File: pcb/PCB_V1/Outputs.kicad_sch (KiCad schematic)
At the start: 21 parts, among them J501 FAN1 / 3.5 mm, J511 FAN2 / 3.5 mm, J521 PUMP 24V / 6W, Q501 AO3400A, Q511 AO3400A, Q521 AO3422

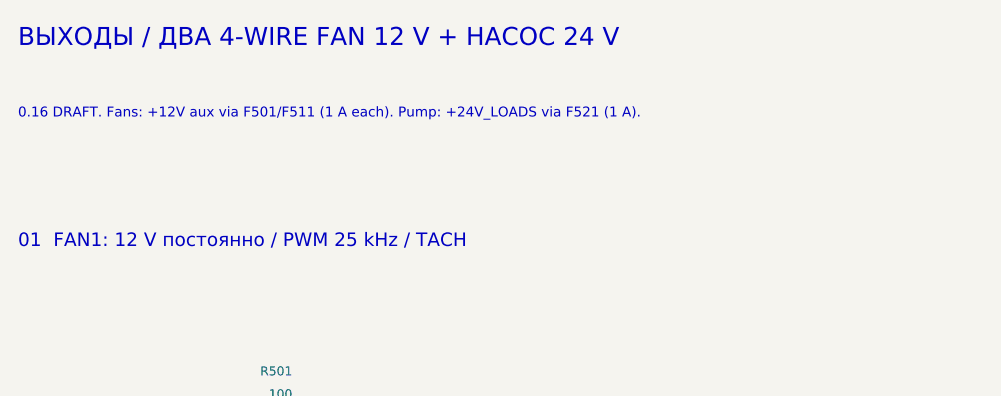
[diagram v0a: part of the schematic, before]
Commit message: pcb: integrate reviewed parts and validate initial 100mm placement
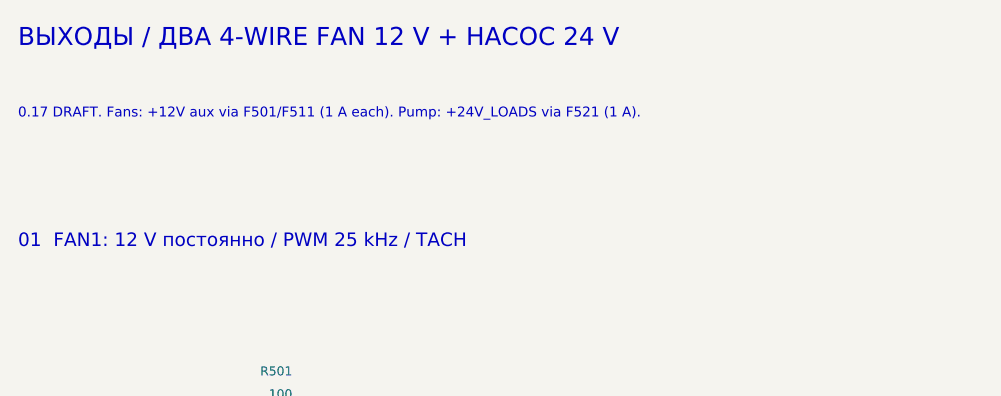
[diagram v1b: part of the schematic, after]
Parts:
- J501, J511: footprint TerminalBlock_Phoenix:TerminalBlock_Phoenix_PT-1,5-4-3.5-H_1x04_P3.50mm_Horizontal -> GrowBox:TerminalBlock_DORABO_DB125-3.5_1x04_P3.50mm_Horizontal
- J521: footprint TerminalBlock_Phoenix:TerminalBlock_Phoenix_PT-1,5-2-3.5-H_1x02_P3.50mm_Horizontal -> GrowBox:TerminalBlock_DORABO_DB125-3.5_1x02_P3.50mm_Horizontal
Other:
- note added: "0.17 DRAFT. Fans: +12V aux via F501/F511 (1 A each). Pump: +24V_LOADS via F521 (1 A)."
- note removed: "0.16 DRAFT. Fans: +12V aux via F501/F511 (1 A each). Pump: +24V_LOADS via F521 (1 A)."
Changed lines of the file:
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@@
 	(title_block
 		(title "04 - Fans (12 V aux) and pump (24 V)")
-		(date "2026-09-27")
-		(rev "0.16-DRAFT")
+		(date "2026-09-28")
+		(rev "0.17-DRAFT")
 		(company "GrowBox controller")
 		(comment 1 "Engineering draft; startup, thermal and fault qualification pending")
@@
 		)
 	)
-	(text "0.16 DRAFT. Fans: +12V aux via F501/F511 (1 A each). Pump: +24V_LOADS via F521 (1 A)."
+	(text "0.17 DRAFT. Fans: +12V aux via F501/F511 (1 A each). Pump: +24V_LOADS via F521 (1 A)."
 		(exclude_from_sim no)
 		(at 20.32 24.13 0)
@@
 			)
 		)
-		(property "Footprint" "TerminalBlock_Phoenix:TerminalBlock_Phoenix_PT-1,5-4-3.5-H_1x04_P3.50mm_Horizontal"
+		(property "Footprint" "GrowBox:TerminalBlock_DORABO_DB125-3.5_1x04_P3.50mm_Horizontal"
 			(at 182.88 60.96 0)
 			(hide yes)
@@
 			)
 		)
-		(property "Footprint" "TerminalBlock_Phoenix:TerminalBlock_Phoenix_PT-1,5-2-3.5-H_1x02_P3.50mm_Horizontal"
+		(property "Footprint" "GrowBox:TerminalBlock_DORABO_DB125-3.5_1x02_P3.50mm_Horizontal"
 			(at 185.42 191.77 0)
 			(hide yes)
@@
 			)
 		)
-		(property "Footprint" "TerminalBlock_Phoenix:TerminalBlock_Phoenix_PT-1,5-4-3.5-H_1x04_P3.50mm_Horizontal"
+		(property "Footprint" "GrowBox:TerminalBlock_DORABO_DB125-3.5_1x04_P3.50mm_Horizontal"
 			(at 381 60.96 0)
 			(hide yes)

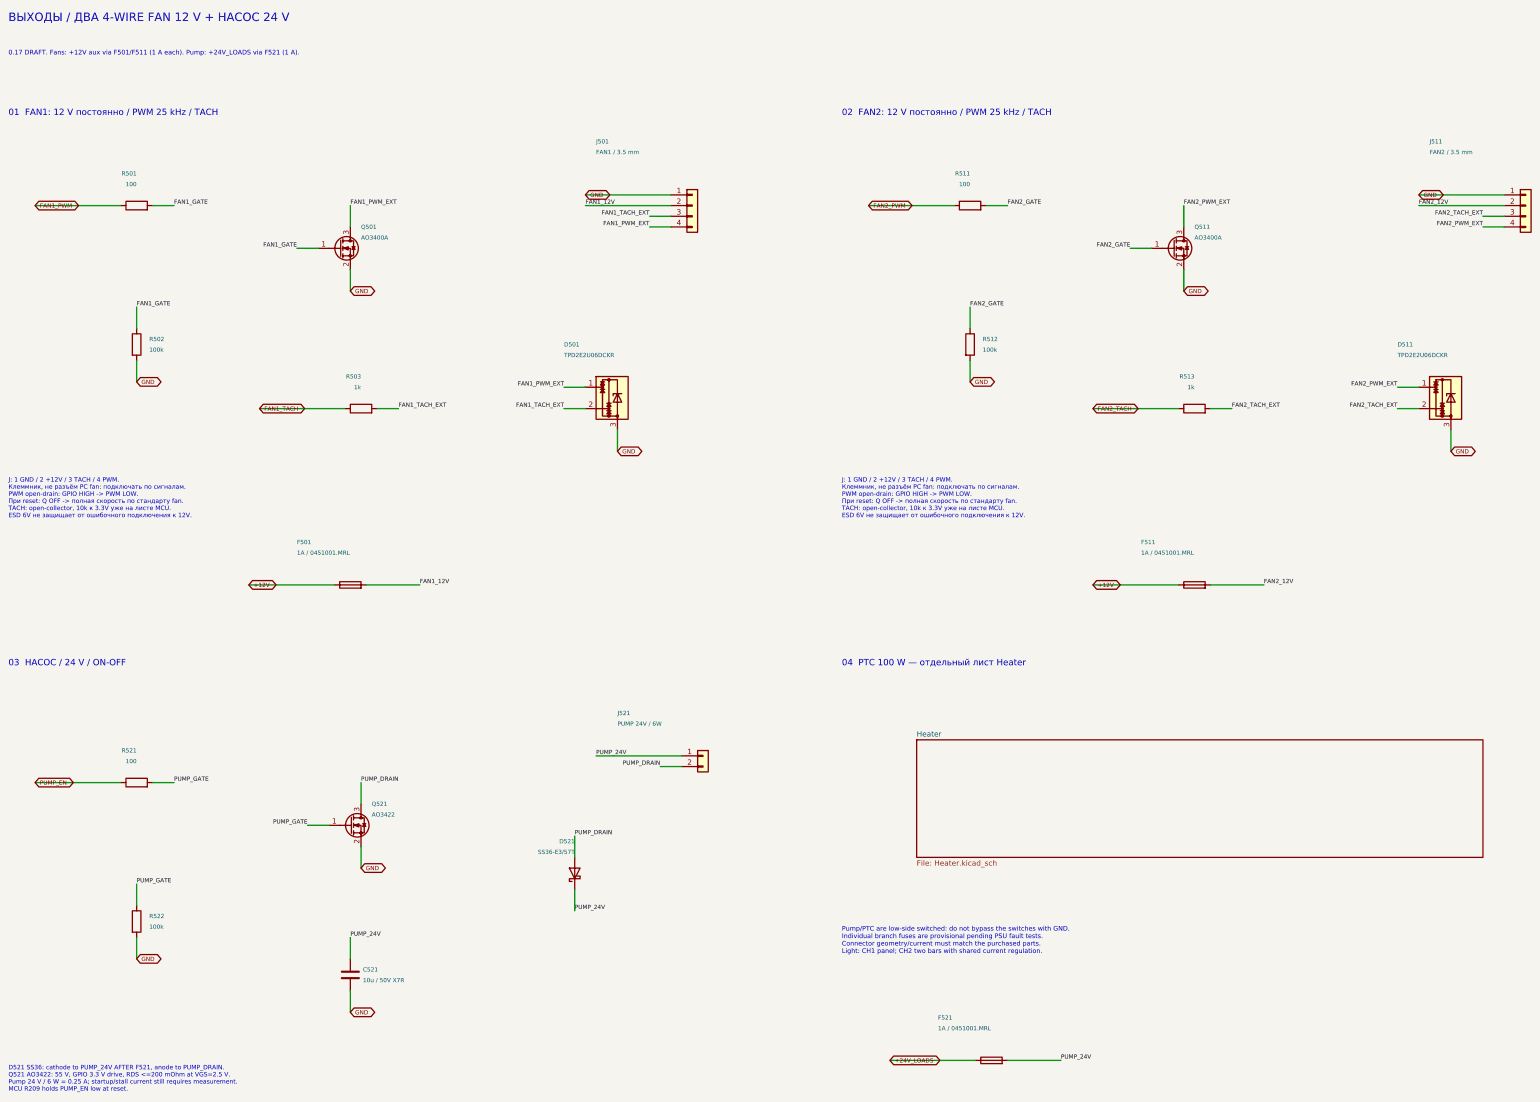
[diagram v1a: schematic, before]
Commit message: pcb: simplify passives and microSD circuitry for revision 0.18
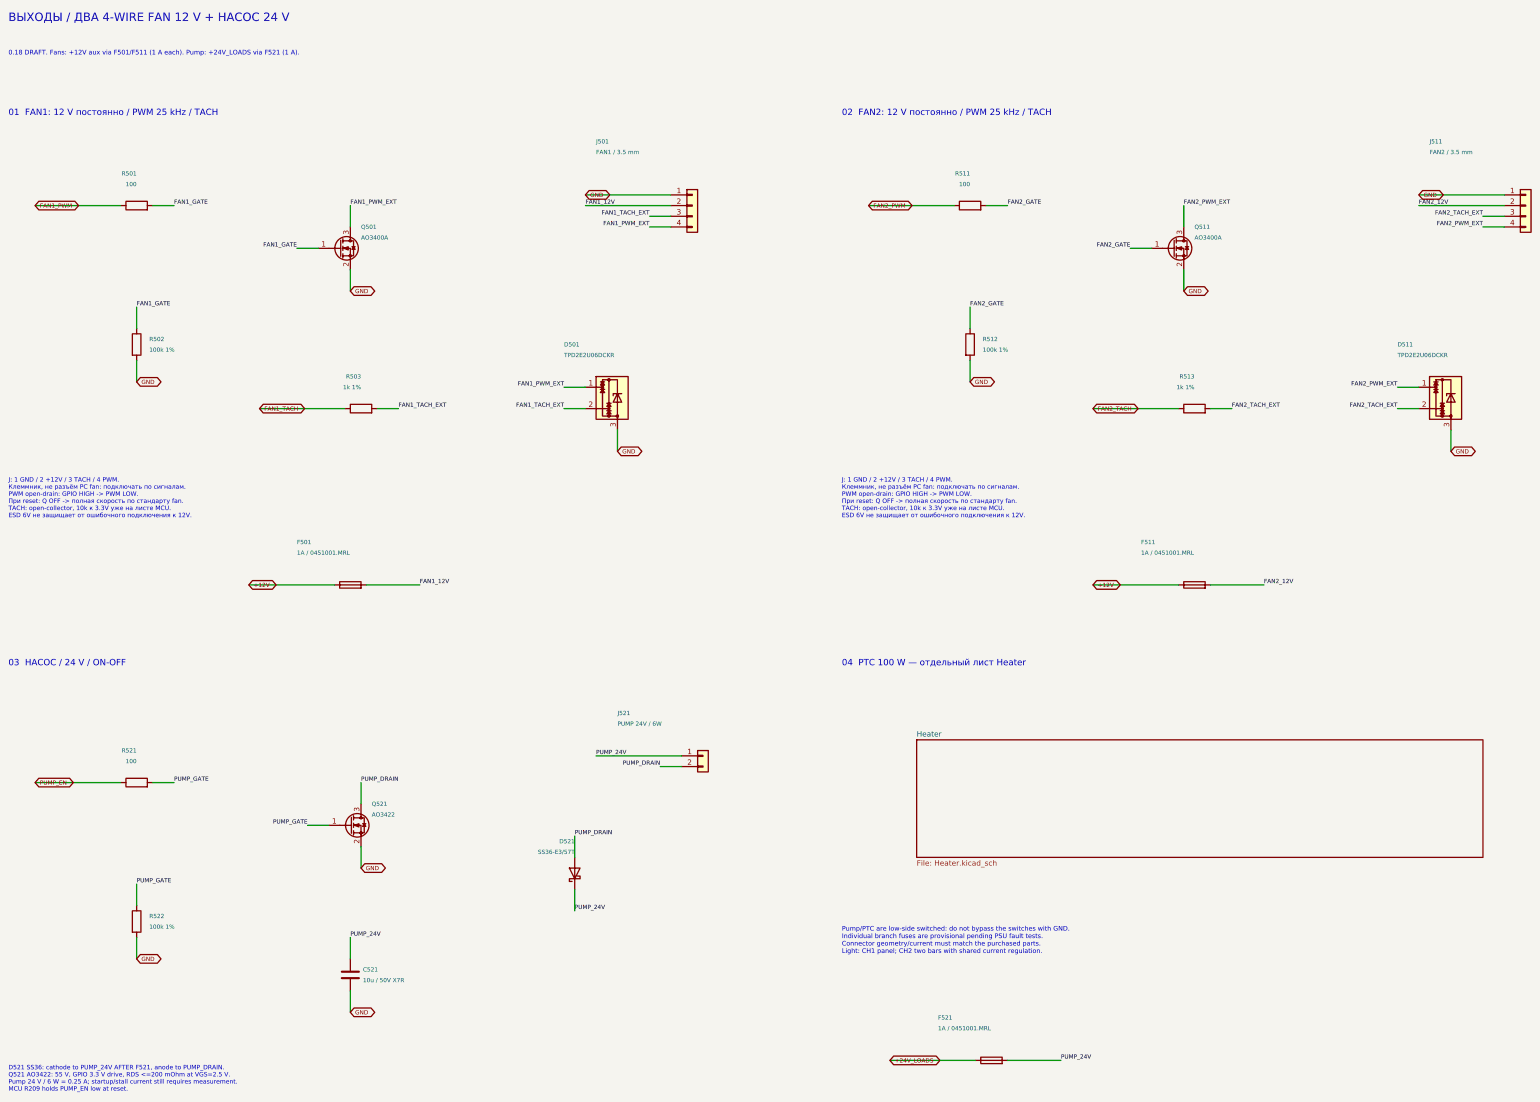
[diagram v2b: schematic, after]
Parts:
- R502, R512, R522: value 100k -> 100k 1%; LCSC (none) -> C25803; MPN (none) -> 0603WAF1003T5E; Manufacturer (none) -> UNI-ROYAL
- R503, R513: value 1k -> 1k 1%; LCSC (none) -> C21190; MPN (none) -> 0603WAF1001T5E; Manufacturer (none) -> UNI-ROYAL
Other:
- note added: "0.18 DRAFT. Fans: +12V aux via F501/F511 (1 A each). Pump: +24V_LOADS via F521 (1 A)."
- note removed: "0.17 DRAFT. Fans: +12V aux via F501/F511 (1 A each). Pump: +24V_LOADS via F521 (1 A)."
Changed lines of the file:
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@@
 	(title_block
 		(title "04 - Fans (12 V aux) and pump (24 V)")
-		(date "2026-09-28")
-		(rev "0.17-DRAFT")
+		(date "2026-09-29")
+		(rev "0.18-DRAFT")
 		(company "GrowBox controller")
-		(comment 1 "Engineering draft; startup, thermal and fault qualification pending")
+		(comment 1 "Simplified prototype; unrouted; hardware qualification pending")
 	)
 	(text "04  PTC 100 W — отдельный лист Heater"
@@
 		)
 	)
-	(text "0.17 DRAFT. Fans: +12V aux via F501/F511 (1 A each). Pump: +24V_LOADS via F521 (1 A)."
+	(text "0.18 DRAFT. Fans: +12V aux via F501/F511 (1 A each). Pump: +24V_LOADS via F521 (1 A)."
 		(exclude_from_sim no)
 		(at 20.32 24.13 0)
@@
 			)
 		)
-		(property "Value" "100k"
+		(property "Value" "100k 1%"
 			(at 53.8 232.41 0)
 			(show_name no)
@@
 					(unit 1)
 				)
+			)
+		)
+		(property "Manufacturer" "UNI-ROYAL"
+			(at 50.8 231.14 0)
+			(hide yes)
+			(show_name no)
+			(do_not_autoplace no)
+			(effects
+				(font
+					(size 1 1)
+				)
+				(justify left)
+			)
+		)
+		(property "MPN" "0603WAF1003T5E"
+			(at 50.8 231.14 0)
+			(hide yes)
+			(show_name no)
+			(do_not_autoplace no)
+			(effects
+				(font
+					(size 1 1)
+				)
+				(justify left)
+			)
+		)
+		(property "LCSC" "C25803"
+			(at 50.8 231.14 0)
+			(hide yes)
+			(show_name no)
+			(do_not_autoplace no)
+			(effects
+				(font
+					(size 1 1)
+				)
+				(justify left)
 			)
 		)
@@
 			)
 		)
-		(property "Value" "100k"
+		(property "Value" "100k 1%"
 			(at 53.8 95.25 0)
 			(show_name no)
@@
 					(unit 1)
 				)
+			)
+		)
+		(property "Manufacturer" "UNI-ROYAL"
+			(at 50.8 93.98 0)
+			(hide yes)
+			(show_name no)
+			(do_not_autoplace no)
+			(effects
+				(font
+					(size 1 1)
+				)
+				(justify left)
+			)
+		)
+		(property "MPN" "0603WAF1003T5E"
+			(at 50.8 93.98 0)
+			(hide yes)
+			(show_name no)
+			(do_not_autoplace no)
+			(effects
+				(font
+					(size 1 1)
+				)
+				(justify left)
+			)
+		)
+		(property "LCSC" "C25803"
+			(at 50.8 93.98 0)
+			(hide yes)
+			(show_name no)
+			(do_not_autoplace no)
+			(effects
+				(font
+					(size 1 1)
+				)
+				(justify left)
 			)
 		)
@@
 			)
 		)
-		(property "Value" "1k"
+		(property "Value" "1k 1%"
 			(at 302.26 104.14 90)
 			(show_name no)
@@
 					(unit 1)
 				)
+			)
+		)
+		(property "Manufacturer" "UNI-ROYAL"
+			(at 302.26 109.22 90)
+			(hide yes)
+			(show_name no)
+			(do_not_autoplace no)
+			(effects
+				(font
+					(size 1 1)
+				)
+				(justify left)
+			)
+		)
+		(property "MPN" "0603WAF1001T5E"
+			(at 302.26 109.22 90)
+			(hide yes)
+			(show_name no)
+			(do_not_autoplace no)
+			(effects
+				(font
+					(size 1 1)
+				)
+				(justify left)
+			)
+		)
+		(property "LCSC" "C21190"
+			(at 302.26 109.22 90)
+			(hide yes)
+			(show_name no)
+			(do_not_autoplace no)
+			(effects
+				(font
+					(size 1 1)
+				)
+				(justify left)
 			)
 		)
@@
 			)
 		)
-		(property "Value" "100k"
+		(property "Value" "100k 1%"
 			(at 251.92 95.25 0)
 			(show_name no)
@@
 					(unit 1)
 				)
+			)
+		)
+		(property "Manufacturer" "UNI-ROYAL"
+			(at 248.92 93.98 0)
+			(hide yes)
+			(show_name no)
+			(do_not_autoplace no)
+			(effects
+				(font
+					(size 1 1)
+				)
+				(justify left)
+			)
+		)
+		(property "MPN" "0603WAF1003T5E"
+			(at 248.92 93.98 0)
+			(hide yes)
+			(show_name no)
+			(do_not_autoplace no)
+			(effects
+				(font
+					(size 1 1)
+				)
+				(justify left)
+			)
+		)
+		(property "LCSC" "C25803"
+			(at 248.92 93.98 0)
+			(hide yes)
+			(show_name no)
+			(do_not_autoplace no)
+			(effects
+				(font
+					(size 1 1)
+				)
+				(justify left)
 			)
 		)
@@
 			)
 		)
-		(property "Value" "1k"
+		(property "Value" "1k 1%"
 			(at 104.14 104.14 90)
 			(show_name no)
@@
 			)
 		)
+		(property "Manufacturer" "UNI-ROYAL"
+			(at 104.14 109.22 90)
+			(hide yes)
+			(show_name no)
+			(do_not_autoplace no)
+			(effects
+				(font
+					(size 1 1)
+				)
+				(justify left)
+			)
+		)
+		(property "MPN" "0603WAF1001T5E"
+			(at 104.14 109.22 90)
+			(hide yes)
+			(show_name no)
+			(do_not_autoplace no)
+			(effects
+				(font
+					(size 1 1)
+				)
+				(justify left)
+			)
+		)
+		(property "LCSC" "C21190"
+			(at 104.14 109.22 90)
+			(hide yes)
+			(show_name no)
+			(do_not_autoplace no)
+			(effects
+				(font
+					(size 1 1)
+				)
+				(justify left)
+			)
+		)
